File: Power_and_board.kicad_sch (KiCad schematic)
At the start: 21 parts, among them U1 AMS1117-3.3

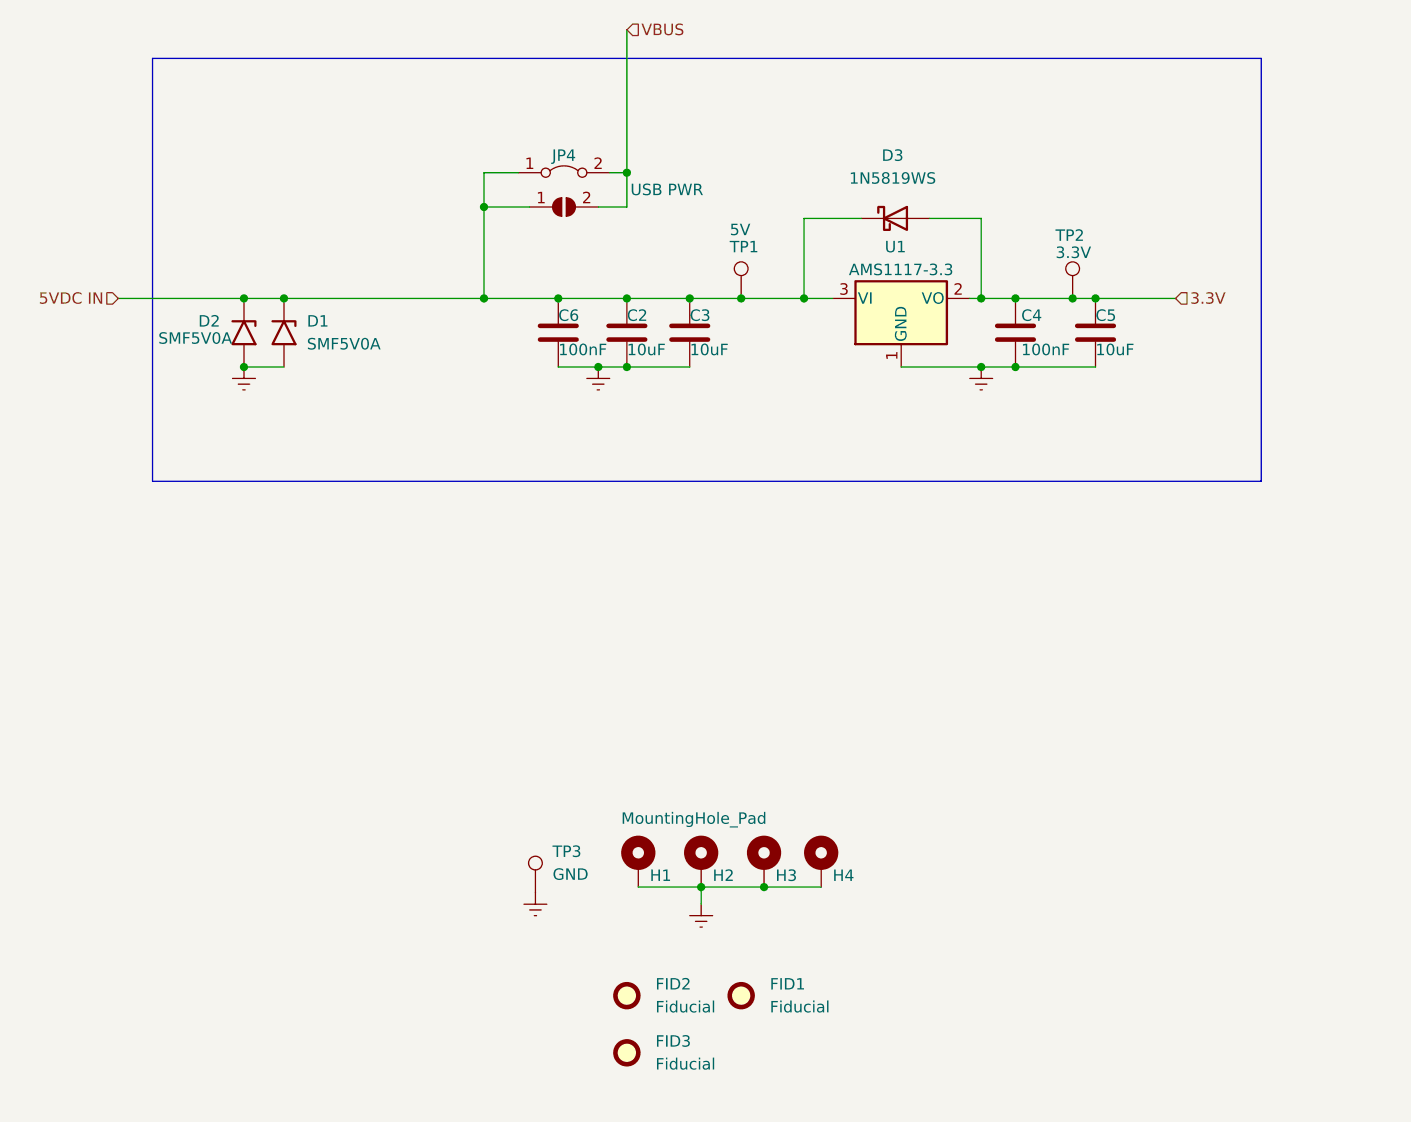
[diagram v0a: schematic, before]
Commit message: some minor cleanup of schematic and layout
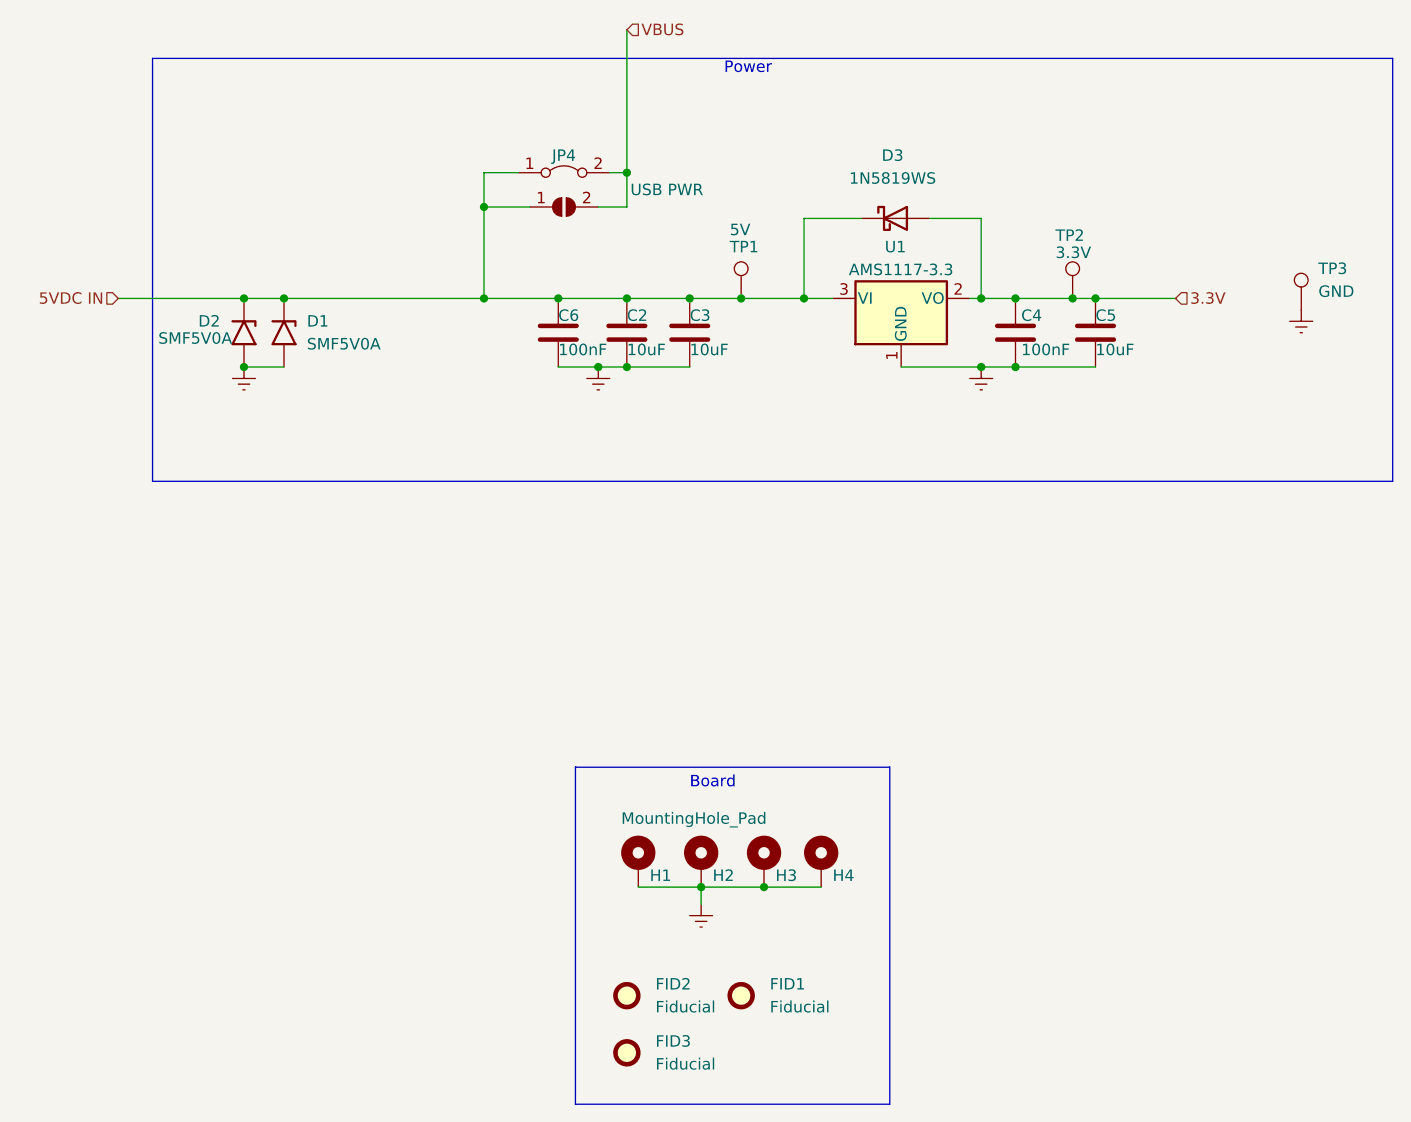
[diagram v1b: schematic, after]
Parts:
- TP1, TP2, TP3: footprint TestPoint:TestPoint_Pad_D2.0mm -> TestPoint:TestPoint_Pad_D1.5mm
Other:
- note added: "Board"
- note added: "Power"
- moved on the sheet: TP3
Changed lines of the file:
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@@
     (stroke (width 0) (type default))
   )
-  (rectangle (start 87.63 73.66) (end 210.82 120.65)
+  (rectangle (start 134.62 152.4) (end 169.545 189.865)
     (stroke (width 0) (type default))
     (fill (type none))
+  )
+  (rectangle (start 87.63 73.66) (end 225.425 120.65)
+    (stroke (width 0) (type default))
+    (fill (type none))
+  )
+  (text "Board" (at 147.32 154.94 0)
+    (effects (font (size 1.27 1.27)) (justify left bottom))
+  )
+  (text "Power" (at 151.13 75.565 0)
+    (effects (font (size 1.27 1.27)) (justify left bottom))
   )
   (hierarchical_label "5VDC IN" (shape input) (at 83.82 100.33 180) (fields_autoplaced)
@@
       (effects (font (size 1.27 1.27)) (justify left))
     )
-    (property "Footprint" "TestPoint:TestPoint_Pad_D2.0mm" (at 158.115 100.33 0)
+    (property "Footprint" "TestPoint:TestPoint_Pad_D1.5mm" (at 158.115 100.33 0)
       (effects (font (size 1.27 1.27)) hide)
     )
@@
     )
   )
-  (symbol (lib_name "Earth_1") (lib_id "power:Earth") (at 130.175 166.37 0) (unit 1)
+  (symbol (lib_name "Earth_1") (lib_id "power:Earth") (at 215.265 101.6 0) (unit 1)
     (in_bom yes) (on_board yes) (dnp no) (fields_autoplaced)
-    (property "Reference" "#PWR013" (at 130.175 172.72 0)
-      (effects (font (size 1.27 1.27)) hide)
-    )
-    (property "Value" "Earth" (at 130.175 170.18 0)
-      (effects (font (size 1.27 1.27)) hide)
-    )
-    (property "Footprint" "" (at 130.175 166.37 0)
-      (effects (font (size 1.27 1.27)) hide)
-    )
-    (property "Datasheet" "~" (at 130.175 166.37 0)
+    (property "Reference" "#PWR013" (at 215.265 107.95 0)
+      (effects (font (size 1.27 1.27)) hide)
+    )
+    (property "Value" "Earth" (at 215.265 105.41 0)
+      (effects (font (size 1.27 1.27)) hide)
+    )
+    (property "Footprint" "" (at 215.265 101.6 0)
+      (effects (font (size 1.27 1.27)) hide)
+    )
+    (property "Datasheet" "~" (at 215.265 101.6 0)
       (effects (font (size 1.27 1.27)) hide)
     )
@@
     )
   )
-  (symbol (lib_id "Connector:TestPoint") (at 130.175 166.37 0) (unit 1)
+  (symbol (lib_id "Connector:TestPoint") (at 215.265 101.6 0) (unit 1)
     (in_bom no) (on_board yes) (dnp no) (fields_autoplaced)
-    (property "Reference" "TP3" (at 132.08 161.7979 0)
-      (effects (font (size 1.27 1.27)) (justify left))
-    )
-    (property "Value" "GND" (at 132.08 164.3379 0)
-      (effects (font (size 1.27 1.27)) (justify left))
-    )
-    (property "Footprint" "TestPoint:TestPoint_Pad_D2.0mm" (at 135.255 166.37 0)
-      (effects (font (size 1.27 1.27)) hide)
-    )
-    (property "Datasheet" "~" (at 135.255 166.37 0)
-      (effects (font (size 1.27 1.27)) hide)
-    )
-    (property "Vendor" "~" (at 130.175 166.37 0)
+    (property "Reference" "TP3" (at 217.17 97.0279 0)
+      (effects (font (size 1.27 1.27)) (justify left))
+    )
+    (property "Value" "GND" (at 217.17 99.5679 0)
+      (effects (font (size 1.27 1.27)) (justify left))
+    )
+    (property "Footprint" "TestPoint:TestPoint_Pad_D1.5mm" (at 220.345 101.6 0)
+      (effects (font (size 1.27 1.27)) hide)
+    )
+    (property "Datasheet" "~" (at 220.345 101.6 0)
+      (effects (font (size 1.27 1.27)) hide)
+    )
+    (property "Vendor" "~" (at 215.265 101.6 0)
       (effects (font (size 1.27 1.27)) hide)
     )
@@
       (effects (font (size 1.27 1.27)) (justify left))
     )
-    (property "Footprint" "TestPoint:TestPoint_Pad_D2.0mm" (at 194.945 100.33 0)
-      (effects (font (size 1.27 1.27)) hide)
-    )
+    (property "Footprint" "TestPoint:TestPoint_Pad_D1.5mm" (at 194.945 100.33 0)
+      (effects (font (size 1.27 1.27)) hide)
+    )

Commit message: organized schematic & added bom
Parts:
- C4, C6: Vendor https://www.lcsc.com/product-detail/Multilayer-Ceramic-Capa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 -> https://jlcpcb.com/partdetail/Yageo-CC0805KRX7R9BB104/C49678
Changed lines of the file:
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@@
   (title_block
     (title "Spotify Reactive IoT LED Strip Driver")
-    (date "2023-08-13")
+    (date "2023-09-16")
     (rev "v1.9.1-a")
     (comment 2 "to the currently playing song on spotify")
@@
       (effects (font (size 1.27 1.27)) hide)
     )
-    (property "Vendor" "https://www.lcsc.com/product-detail/Multilayer-Ceramic-Capacitors-MLCC-SMD-SMT_FH-Guangdong-Fenghua-Advanced-Tech-0805B104K500NT_C38141.html" (at 132.715 104.14 0)
+    (property "Vendor" "https://jlcpcb.com/partdetail/Yageo-CC0805KRX7R9BB104/C49678" (at 132.715 104.14 0)
       (effects (font (size 1.27 1.27)) hide)
     )
@@
       (effects (font (size 1.27 1.27)) hide)
     )
-    (property "Vendor" "https://www.lcsc.com/product-detail/Multilayer-Ceramic-Capacitors-MLCC-SMD-SMT_FH-Guangdong-Fenghua-Advanced-Tech-0805B104K500NT_C38141.html" (at 183.515 104.14 0)
-      (effects (font (size 1.27 1.27)) hide)
-    )
+    (property "Vendor" "https://jlcpcb.com/partdetail/Yageo-CC0805KRX7R9BB104/C49678" (at 183.515 104.14 0)
+      (effects (font (size 1.27 1.27)) hide)
+    )

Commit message: final modifications, cleanup, added v2.0 photos as ordered
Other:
- title: Spotify Reactive IoT LED Strip Driver -> Spotify Neopixel Visualizer
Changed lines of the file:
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@@
   (paper "A4")
   (title_block
-    (title "Spotify Reactive IoT LED Strip Driver")
-    (date "2023-09-16")
-    (rev "v1.9.1-a")
-    (comment 2 "to the currently playing song on spotify")
-    (comment 3 "A modular, internet connected LED strip driver that reacts ")
+    (title "Spotify Neopixel Visualizer")
+    (date "2023-09-17")
+    (rev "v2.0")
+    (comment 2 "the Spotify API to react to the currently playing song on Spotify")
+    (comment 3 "A modular, internet connected LED strip driver that uses ")
   )
   (junction (at 132.715 100.33) (diameter 0) (color 0 0 0 0)

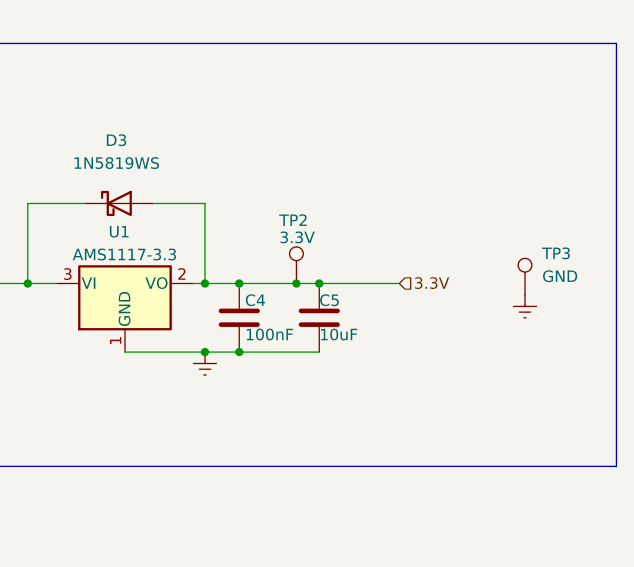
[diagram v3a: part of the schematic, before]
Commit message: Moved button labels and multiple minor modifications
* Implemented Orion's suggestion for replacing 10uF cap on reset button
  with 100nF.
* Moved silkscreen for both buttons underneath and moved jtag label.
* Added labels to both power and status LEDs.
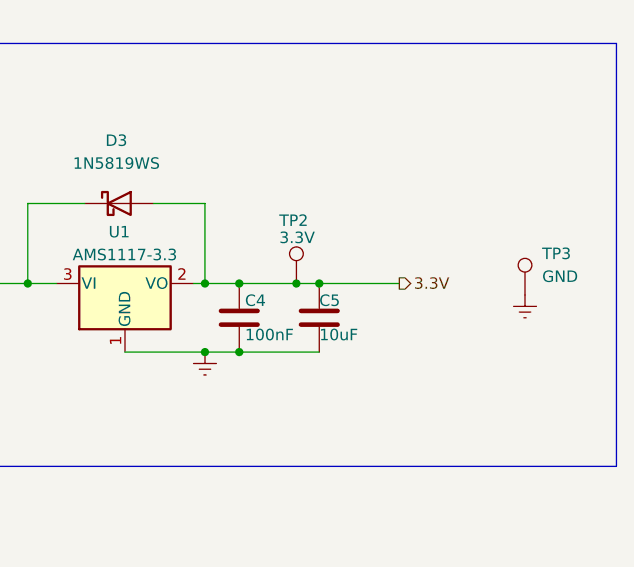
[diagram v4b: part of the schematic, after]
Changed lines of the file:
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@@
     (effects (font (size 1.27 1.27)) (justify left))
   )
-  (hierarchical_label "3.3V" (shape input) (at 201.295 100.33 0) (fields_autoplaced)
+  (hierarchical_label "3.3V" (shape output) (at 201.295 100.33 0) (fields_autoplaced)
     (effects (font (size 1.27 1.27)) (justify left))
   )

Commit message: lots of small changes. Schematic updated with mic, layout not yet
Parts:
- added J7: PWR_HEADER, Connector_Wire:SolderWire-0.1sqmm_1x02_P3.6mm_D0.4mm_OD1mm, symbol Connector_Generic:Conn_01x02
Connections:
- net 5VDC IN: now also J7.2 (Pin_2)
- net Earth: now also J7.1 (Pin_1)
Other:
- note added: "Additional 5V Power header for the extra power and ground lines that come with WS2812B LED strips."
- note added: "Allows disconnect of USB's VBUS from the Board's VCC, to prevent feedback when programming the board while it's plugged in."
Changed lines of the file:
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@@
   (title_block
     (title "Spotify Neopixel Visualizer")
-    (date "2023-09-17")
-    (rev "v2.0")
-    (comment 2 "the Spotify API to react to the currently playing song on Spotify")
+    (date "2023-10-08")
+    (rev "v2.0.9")
+    (comment 2 "the Spotify API to react to the currently playing song on Spotify.")
     (comment 3 "A modular, internet connected LED strip driver that uses ")
   )
@@
   (junction (at 189.865 100.33) (diameter 0) (color 0 0 0 0)
   )
+  (junction (at 154.305 100.33) (diameter 0) (color 0 0 0 0)
+  )
   (junction (at 183.515 107.95) (diameter 0) (color 0 0 0 0)
   )
@@
     (stroke (width 0) (type default))
   )
-  (wire (pts (xy 153.035 100.33) (xy 160.02 100.33))
+  (wire (pts (xy 153.035 100.33) (xy 154.305 100.33))
     (stroke (width 0) (type default))
   )
@@
     (stroke (width 0) (type default))
   )
+  (wire (pts (xy 154.305 116.205) (xy 154.305 117.475))
+    (stroke (width 0) (type default))
+  )
   (wire (pts (xy 124.46 90.17) (xy 129.54 90.17))
     (stroke (width 0) (type default))
@@
     (stroke (width 0) (type default))
   )
+  (wire (pts (xy 154.305 100.33) (xy 160.02 100.33))
+    (stroke (width 0) (type default))
+  )
   (wire (pts (xy 183.515 107.95) (xy 192.405 107.95))
     (stroke (width 0) (type default))
   )
+  (wire (pts (xy 154.305 100.33) (xy 154.305 113.665))
+    (stroke (width 0) (type default))
+  )
   (wire (pts (xy 83.82 100.33) (xy 97.79 100.33))
     (stroke (width 0) (type default))
@@
     (fill (type none))
   )
-  (rectangle (start 87.63 73.66) (end 225.425 120.65)
+  (rectangle (start 87.63 73.66) (end 225.425 125.095)
     (stroke (width 0) (type default))
     (fill (type none))
+  )
+  (text "Allows disconnect of USB's VBUS \nfrom the Board's VCC, to prevent \nfeedback when programming the \nboard while it's plugged in. "
+    (at 113.665 81.915 0)
+    (effects (font (size 1 1)) (justify left bottom))
   )
   (text "Board" (at 147.32 154.94 0)
     (effects (font (size 1.27 1.27)) (justify left bottom))
+  )
+  (text "Additional 5V Power header for\nthe extra power and ground lines \nthat come with WS2812B LED strips. "
+    (at 157.48 123.19 0)
+    (effects (font (size 1 1)) (justify left bottom))
   )
   (text "Power" (at 151.13 75.565 0)
@@
       (effects (font (size 1.27 1.27)) hide)
     )
-    (property "Datasheet" "~" (at 192.405 104.14 0)
-      (effects (font (size 1.27 1.27)) hide)
-    )
-    (property "Description" "" (at 192.405 104.14 0)
+    (property "Datasheet" "" (at 192.405 104.14 0)
+      (effects (font (size 1.27 1.27)) hide)
+    )
+    (property "Description" "16V 10uF 0805 Ceramic Capacitor SMD" (at 192.405 104.14 0)
       (effects (font (size 1.27 1.27)) hide)
     )
@@
       (effects (font (size 1.27 1.27)) hide)
     )
-    (property "Datasheet" "~" (at 147.32 104.14 0)
-      (effects (font (size 1.27 1.27)) hide)
-    )
-    (property "Description" "" (at 147.32 104.14 0)
+    (property "Datasheet" "" (at 147.32 104.14 0)
+      (effects (font (size 1.27 1.27)) hide)
+    )
+    (property "Description" "16V 10uF 0805 Ceramic Capacitor SMD" (at 147.32 104.14 0)
       (effects (font (size 1.27 1.27)) hide)
     )
@@
       (effects (font (size 1.27 1.27)) hide)
     )
+    (property "Description" "9.2V 6.4V 5V SMF TVS " (at 97.79 104.14 0)
+      (effects (font (size 1.27 1.27)) hide)
+    )
     (pin "1")
     (pin "2")
@@
         (path "/745f5767-ebad-4719-b66e-073bc90db4bc"
           (reference "D5") (unit 1)
+        )
+      )
+    )
+  )
+  (symbol (lib_id "power:Earth") (at 154.305 117.475 0) (unit 1)
+    (in_bom yes) (on_board yes) (dnp no) (fields_autoplaced)
+    (property "Reference" "#PWR036" (at 154.305 123.825 0)
+      (effects (font (size 1.27 1.27)) hide)
+    )
+    (property "Value" "Earth" (at 154.305 121.285 0)
+      (effects (font (size 1.27 1.27)) hide)
+    )
+    (property "Footprint" "" (at 154.305 117.475 0)
+      (effects (font (size 1.27 1.27)) hide)
+    )
+    (property "Datasheet" "~" (at 154.305 117.475 0)
+      (effects (font (size 1.27 1.27)) hide)
+    )
+    (pin "1")
+    (instances
+      (project "iot_led_strip_pcb"
+        (path "/745f5767-ebad-4719-b66e-073bc90db4bc/cfe13250-7fa5-4f24-964e-9463793dd38d"
+          (reference "#PWR036") (unit 1)
+        )
+        (path "/745f5767-ebad-4719-b66e-073bc90db4bc"
+          (reference "#PWR012") (unit 1)
         )
       )
@@
       (effects (font (size 1.27 1.27)) hide)
     )
-    (property "Datasheet" "~" (at 140.335 104.14 0)
-      (effects (font (size 1.27 1.27)) hide)
-    )
-    (property "Description" "" (at 140.335 104.14 0)
+    (property "Datasheet" "" (at 140.335 104.14 0)
+      (effects (font (size 1.27 1.27)) hide)
+    )
+    (property "Description" "16V 10uF 0805 Ceramic Capacitor SMD" (at 140.335 104.14 0)
       (effects (font (size 1.27 1.27)) hide)
     )
@@
         (path "/745f5767-ebad-4719-b66e-073bc90db4bc"
           (reference "C8") (unit 1)
+        )
+      )
+    )
+  )
+  (symbol (lib_id "Connector_Generic:Conn_01x02") (at 159.385 116.205 0) (mirror x) (unit 1)
+    (in_bom yes) (on_board yes) (dnp no)
+    (property "Reference" "J7" (at 162.56 116.205 0)
+      (effects (font (size 1.27 1.27)) (justify left))
+    )
+    (property "Value" "PWR_HEADER" (at 162.56 113.665 0)
+      (effects (font (size 1.27 1.27)) (justify left))
+    )
+    (property "Footprint" "Connector_Wire:SolderWire-0.1sqmm_1x02_P3.6mm_D0.4mm_OD1mm" (at 159.385 116.205 0)
+      (effects (font (size 1.27 1.27)) hide)
+    )
+    (property "Datasheet" "~" (at 159.385 116.205 0)
+      (effects (font (size 1.27 1.27)) hide)
+    )
+    (pin "1")
+    (pin "2")
+    (instances
+      (project "iot_led_strip_pcb"
+        (path "/745f5767-ebad-4719-b66e-073bc90db4bc/cfe13250-7fa5-4f24-964e-9463793dd38d"
+          (reference "J7") (unit 1)
         )
       )
@@
       (effects (font (size 1.27 1.27)) hide)
     )
+    (property "Description" "9.2V 6.4V 5V SMF TVS " (at 102.235 104.14 0)
+      (effects (font (size 1.27 1.27)) hide)
+    )
     (pin "1")
     (pin "2")
@@
       (effects (font (size 1.27 1.27)) hide)
     )
-    (property "Datasheet" "~" (at 132.715 104.14 0)
+    (property "Datasheet" "" (at 132.715 104.14 0)
       (effects (font (size 1.27 1.27)) hide)
     )
@@
     )
     (property "LCSC" "C49678" (at 132.715 104.14 0)
+      (effects (font (size 1.27 1.27)) hide)
+    )
+    (property "Description" "100nF 50V X7R ±10% 0805 Ceramic Cap SMD" (at 132.715 104.14 0)
       (effects (font (size 1.27 1.27)) hide)
     )
@@
       (effects (font (size 1.27 1.27)) hide)
     )
-    (property "Datasheet" "~" (at 170.18 91.44 0)
+    (property "Datasheet" "" (at 170.18 91.44 0)
       (effects (font (size 1.27 1.27)) hide)
     )
     (property "LCSC" "C191023" (at 170.18 91.44 0)
+      (effects (font (size 1.27 1.27)) hide)
+    )
+    (property "Description" "40V 600mV@1A 1A SOD-323 Schottky Barrier Diode" (at 170.18 91.44 0)
       (effects (font (size 1.27 1.27)) hide)
     )
@@
       (effects (font (size 1.27 1.27)) hide)
     )
-    (property "Datasheet" "~" (at 183.515 104.14 0)
+    (property "Datasheet" "" (at 183.515 104.14 0)
       (effects (font (size 1.27 1.27)) hide)
     )
@@
       (effects (font (size 1.27 1.27)) hide)
     )
+    (property "Description" "100nF 50V X7R ±10% 0805 Ceramic Cap SMD" (at 183.515 104.14 0)
+      (effects (font (size 1.27 1.27)) hide)
+    )
